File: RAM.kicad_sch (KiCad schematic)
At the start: 294 parts, among them J1 Conn_01x50, J2 JTAG_01x06, J3 Conn_01x03_Male, U10 W25Q128JVS, U11 TPS62823DLC, U12 TPS62823DLC, U13 TPS62823DLC, U14 TPS62823DLC, U16 TPS62823DLC, U17 Si52112-B5-GM2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

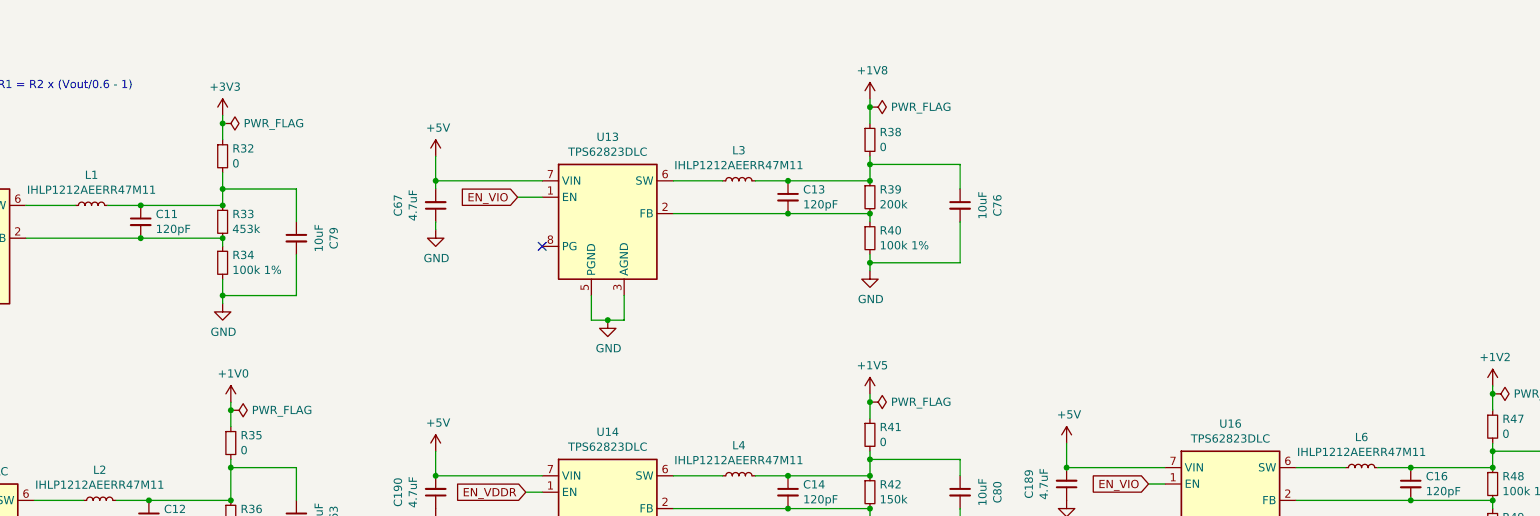
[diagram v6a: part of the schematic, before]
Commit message: schematic: minor cleanups
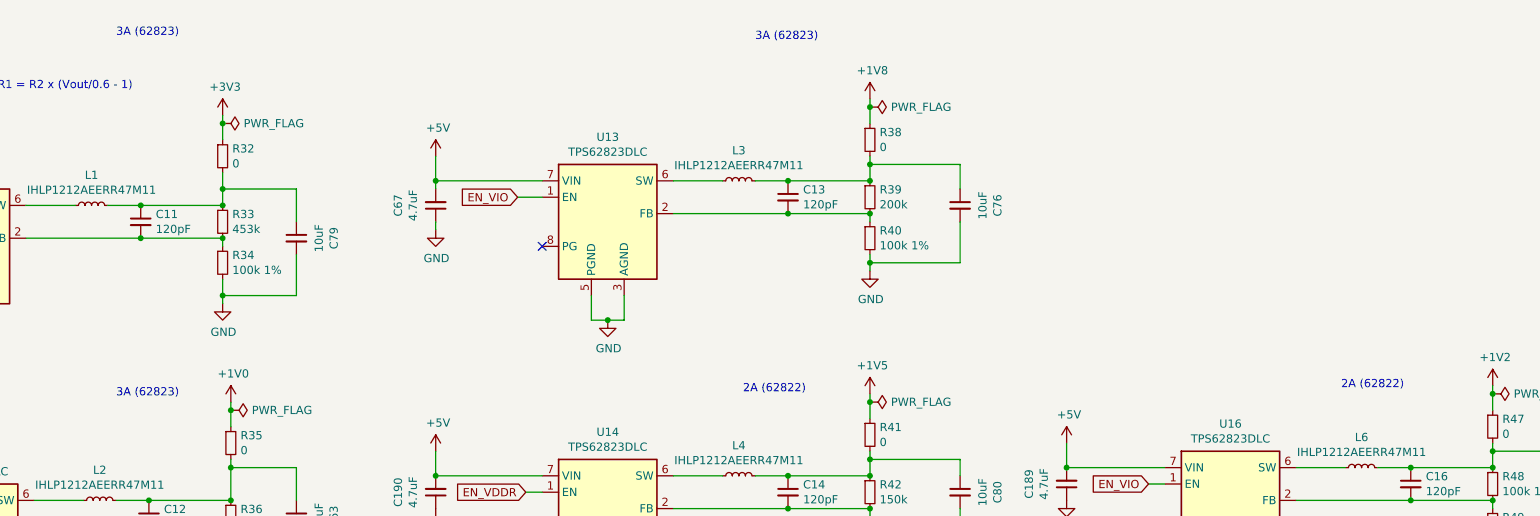
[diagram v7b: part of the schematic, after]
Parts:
- J2: Manufacturer Sullins -> (none); Manufacturer_No SMH100-LPSE -> (none)
- R36, U2: Checked (none) -> y
- R44, R45, R46: Manufacturer_No AC0402FR-070RL -> (none)
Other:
- note added: "2A (62822)"
- note added: "3A (62823)"
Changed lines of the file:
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@@
     (effects (font (size 1.27 1.27)) (justify left bottom))
   )
+  (text "3A (62823)" (at 711.2 60.325 0)
+    (effects (font (size 1.27 1.27)) (justify left bottom))
+  )
   (text "IS43TR16512B-125KBLI" (at 243.84 252.73 0)
     (effects (font (size 1.27 1.27)) (justify left bottom))
@@
     (effects (font (size 1.27 1.27)) (justify left bottom))
   )
+  (text "3A (62823)" (at 810.26 60.96 0)
+    (effects (font (size 1.27 1.27)) (justify left bottom))
+  )
   (text "Config Flash" (at 589.28 426.72 0)
     (effects (font (size 1.27 1.27)) (justify left bottom))
@@
     (effects (font (size 1.27 1.27)) (justify left bottom))
   )
+  (text "3A (62823)" (at 711.2 116.205 0)
+    (effects (font (size 1.27 1.27)) (justify left bottom))
+  )
   (text "PWM" (at 720.725 631.19 0)
     (effects (font (size 1.27 1.27)) (justify left bottom))
@@
     (effects (font (size 1.27 1.27)) (justify left bottom))
   )
+  (text "2A (62822)" (at 808.355 115.57 0)
+    (effects (font (size 1.27 1.27)) (justify left bottom))
+  )
   (text "Config: 1110 (RGMII)" (at 932.18 389.89 0)
     (effects (font (size 1.27 1.27)) (justify left bottom))
@@
     (effects (font (size 1.27 1.27)) (justify left bottom))
   )
+  (text "2A (62822)" (at 901.065 114.935 0)
+    (effects (font (size 1.27 1.27)) (justify left bottom))
+  )
   (text "RESET" (at 720.725 623.57 0)
     (effects (font (size 1.27 1.27)) (justify left bottom))
@@
       (effects (font (size 1.27 1.27)) hide)
     )
+    (property "Checked" "y" (id 6) (at 113.03 147.32 0)
+      (effects (font (size 1.27 1.27)) hide)
+    )
     (pin "AA21")
     (pin "AA22")
@@
       (effects (font (size 1.27 1.27)) hide)
     )
+    (property "Checked" "y" (id 6) (at 260.35 147.32 0)
+      (effects (font (size 1.27 1.27)) hide)
+    )
     (pin "AA21")
     (pin "AA22")
@@
       (effects (font (size 1.27 1.27)) hide)
     )
+    (property "Checked" "y" (id 6) (at 551.18 166.37 0)
+      (effects (font (size 1.27 1.27)) hide)
+    )
     (pin "AA21")
     (pin "AA22")
@@
       (effects (font (size 1.27 1.27)) hide)
     )
+    (property "Checked" "y" (id 6) (at 400.05 147.32 0)
+      (effects (font (size 1.27 1.27)) hide)
+    )
     (pin "AA21")
     (pin "AA22")
@@
       (effects (font (size 1.27 1.27)) hide)
     )
+    (property "Checked" "y" (id 6) (at 127 332.74 0)
+      (effects (font (size 1.27 1.27)) hide)
+    )
     (pin "AA21")
     (pin "AA22")
@@
       (effects (font (size 1.27 1.27)) hide)
     )
+    (property "Checked" "y" (id 6) (at 427.99 316.23 0)
+      (effects (font (size 1.27 1.27)) hide)
+    )
     (pin "AA21")
     (pin "AA22")
@@
       (effects (font (size 1.27 1.27)) hide)
     )
+    (property "Checked" "y" (id 6) (at 427.99 378.46 0)
+      (effects (font (size 1.27 1.27)) hide)
+    )
     (pin "AA21")
     (pin "AA22")
@@
       (effects (font (size 1.27 1.27)) hide)
     )
+    (property "Checked" "y" (id 6) (at 427.99 455.93 0)
+      (effects (font (size 1.27 1.27)) hide)
+    )
     (pin "AA21")
     (pin "AA22")
@@
       (effects (font (size 1.27 1.27)) hide)
     )
+    (property "Checked" "y" (id 6) (at 728.98 134.62 0)
+      (effects (font (size 1.27 1.27)) hide)
+    )
     (pin "1")
     (pin "2")
@@
       (effects (font (size 1.27 1.27)) hide)
     )
-    (property "Manufacturer" "Sullins" (id 4) (at 471.17 406.4 0)
+    (property "Manufacturer" "" (id 4) (at 471.17 406.4 0)
       (effects (font (size 1.27 1.27)) hide)
     )
-    (property "Manufacturer_No" "SMH100-LPSE" (id 5) (at 471.17 406.4 0)
+    (property "Manufacturer_No" "" (id 5) (at 471.17 406.4 0)
       (effects (font (size 1.27 1.27)) hide)
     )
@@
       (effects (font (size 1.27 1.27)) hide)
     )
-    (property "Manufacturer_No" "AC0402FR-070RL" (id 6) (at 194.31 134.62 0)
+    (property "Manufacturer_No" "" (id 6) (at 194.31 134.62 0)
       (effects (font (size 1.27 1.27)) hide)
     )
@@
       (effects (font (size 1.27 1.27)) hide)
     )
-    (property "Manufacturer_No" "AC0402FR-070RL" (id 6) (at 195.58 137.16 0)
+    (property "Manufacturer_No" "" (id 6) (at 195.58 137.16 0)
       (effects (font (size 1.27 1.27)) hide)
     )
@@
       (effects (font (size 1.27 1.27)) hide)
     )
-    (property "Manufacturer_No" "AC0402FR-070RL" (id 6) (at 187.96 132.08 0)
+    (property "Manufacturer_No" "" (id 6) (at 187.96 132.08 0)
       (effects (font (size 1.27 1.27)) hide)
     )

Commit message: clean up schematics
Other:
- note added: "50P FPC for RGB-EDP DISPLAY"
- note added: "BOOT MODE JUMPER"
- note added: "CONFIG SPI FLASH"
- note added: "DIFF CLOCK (for PCIe)"
- note added: "ETHERNET PHY"
- note added: "Extra GPIOs"
- note added: "HDMI DISPLAY"
- note added: "JTAG ETC"
- note added: "KINTEX BANKS"
- note added: "KINTEX GTX"
- note added: "KINTEX POWER"
- note added: "POWER"
- note removed: "50p FPC"
- note removed: "Config Flash"
- note removed: "HDMI"
- note removed: "TODO: - [x] FPC port to ANX9807 - [x] wire up USB host directly and confirm LiteX compat. - test SATA with existing module - test audio with existing module"
- note removed: "TODO: bead"
- note removed: "for later: direct HDMI2.0 possible with TDP158"
- note removed: "https://www.win-source.net/embedded-fpgasfield-programmable-gatearray-xc7k160t-2ffg676i.html"
- moved on the sheet: C1, C10, C100, C101, C102, C103, C104, C105, C106, C107, C108, C109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
